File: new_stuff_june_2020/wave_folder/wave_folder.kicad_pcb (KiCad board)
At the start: 2 copper layers, 99.1 x 99.1 mm, 91 parts, among them J1 signal_port, J2 CV_port, J3 ring_mod_port, J4 power_in_connector, U1 SSM2164, U2 TL072, U3 TL072, U4 TL072, U5 AD534

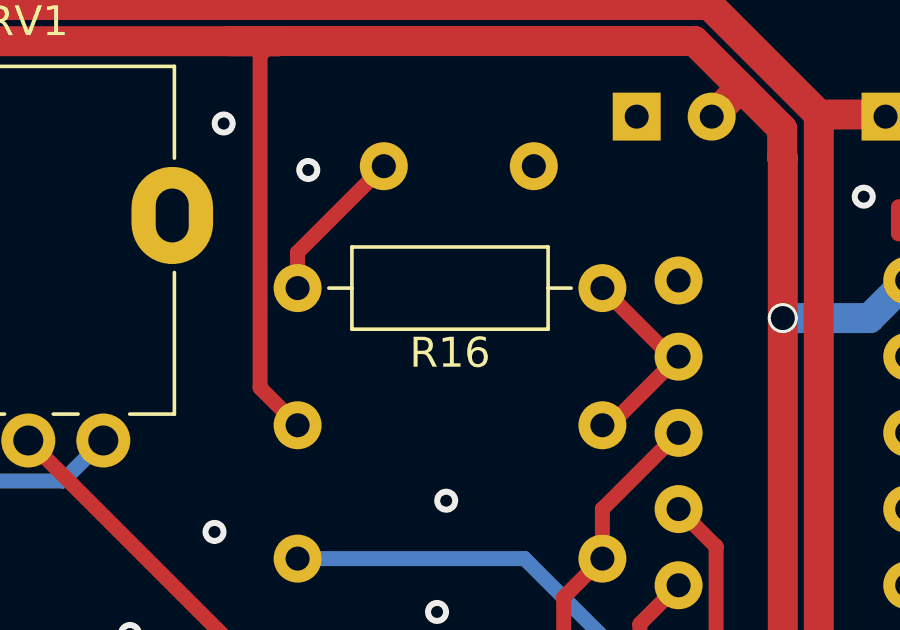
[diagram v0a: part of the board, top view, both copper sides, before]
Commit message: fix resistor on wrong side of pcb
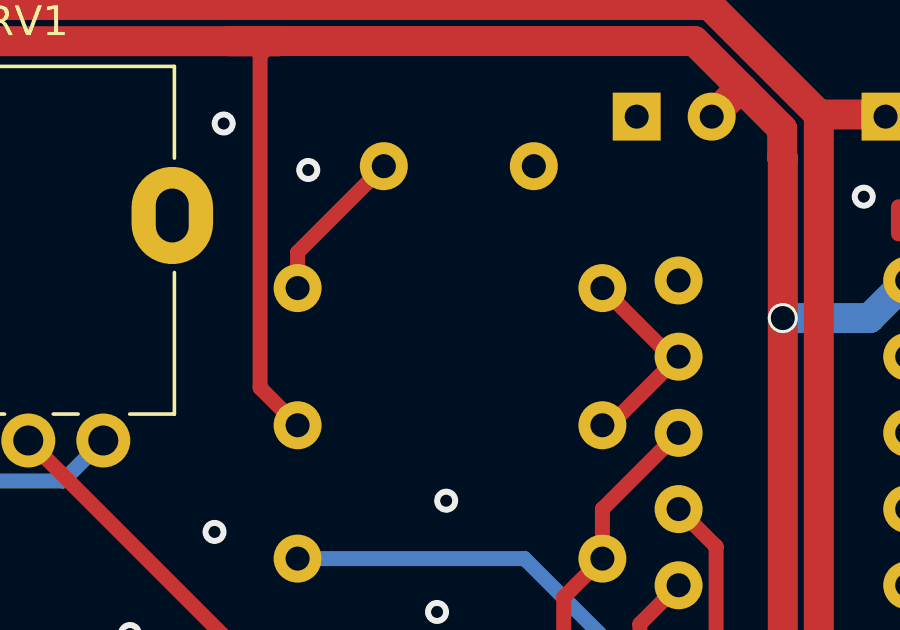
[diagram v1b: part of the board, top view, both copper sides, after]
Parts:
- R16: moved to B.Cu
